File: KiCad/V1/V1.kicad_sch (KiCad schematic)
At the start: 3 parts, among them U1 74LS132

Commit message: kicad scematic
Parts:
- removed R_load: R, symbol Device:R
- added C1, C2, C3, C5, C6, C7, C8: C, symbol Device:C
- added C4: 20p, symbol Device:C
- added L1, L2: L, symbol Device:L
- added R1: R, symbol Device:R
- added R2, R3: 100, symbol Device:R
- added R4, R5: 250, symbol Device:R
- added R6, R7: 0, symbol Device:R
- added R8: NOMCT16031001AT1, NOMC16_VIS, symbol 2024-11-17_18-44-26:NOMCT16031001AT1
- added RV1: R_Potentiometer, symbol Device:R_Potentiometer
- added RV2: 1k, symbol Device:R_Potentiometer
- added U2, U3: OPA2677IDDA, DDA8_3X2P49, symbol 2024-11-17_16-46-04:OPA2677IDDA
- added U4: OPA855QDSGRQ1, WSON8_DSG_TEX, symbol 2024-11-17_18-04-17:OPA855QDSGRQ1
- renumbered R_shutn to R_shutn1
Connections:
- net V_sens: now reaches U1.1
- net V_sens: now also R8.1, U4.6 (OUT)
- net V_ref: now reaches U1.2
- net at U1.3: now also RV2.2
- net -Shunt: now reaches R_shutn1.2
- net -Shunt: now also R8.2
- net Filter/Filter_OUT renamed +Shunt
- net +Shunt: now also L2.2, R8.3
- new net: R2.1, R3.2, U2.2 (INA-)
- new net: C1.1, R1.1
- new net: L1.2, L2.1, R1.2
- new net: R8.13, R8.14, U4.4 (IN+)
- new net: R8.15, R8.16, U4.3 (IN-)
- new net: R6.2, R7.1, U3.4 (VS-)
- new net: R4.1, RV1.1, U2.3 (INA+)
- new net: C4.2, RV1.2, U2.7 (OUTB), U3.2 (INA-)
- new net: R4.2, R5.2, U2.1 (OUTA)
- new net: C4.1, R5.1, U2.6 (INB-)
- new net +5V: C2.2, C3.2, C5.2, C6.2, C7.2, C8.2, R3.1, U2.8 (VS+), U3.7 (OUTB), U4.7 (VS+)
- new net -1V: R6.1
- new net Controll PWM: U3.1 (OUTA)
- new net GND: C1.2, C2.1, C3.1, C5.1, C6.1, C7.1, C8.1, R2.2, R7.2, R8.4, RV2.3, U2.4 (VS-), U2.5 (INB+), U2.EPAD, U3.8 (VS+), U4.5 (VS-), U4.9 (EPAD)
- new net PWM: L1.1
- new net V_Controll: U3.3 (INA+)
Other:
- removed sheet Current Sense
- removed sheet Driver
- removed sheet Filter
- removed sheet PWM Generator
- note added: "Controller"
- note added: "Filter and Sensor"
- note added: "PWM Generator"
- moved on the sheet: R_shutn1, U1A

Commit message: asdaslkwrjhsoid7ty
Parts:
- C1: value C -> 70p; footprint (none) -> Capacitor_SMD:C_0402_1005Metric
- C2, C3, C4, C5, C6, C7, C8: footprint (none) -> Capacitor_SMD:C_0402_1005Metric
- L1, L2: value L -> 1u
- R1: value R -> 200
- R2, R3, R4, R5: footprint (none) -> Resistor_SMD:R_0402_1005Metric
- R6, R7: footprint (none) -> Resistor_SMD:R_0805_2012Metric
- R_shutn1: value R -> 0.1
- U2, U3: footprint DDA8_3X2P49 -> footprints:DDA8_3X2P49
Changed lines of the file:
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@@
 			)
 		)
-		(property "Footprint" ""
+		(property "Footprint" "Resistor_SMD:R_0402_1005Metric"
 			(at 44.45 202.692 90)
 			(effects
@@
 			)
 		)
-		(property "Value" "C"
+		(property "Value" "70p"
 			(at 49.53 78.7399 0)
 			(effects
@@
 			)
 		)
-		(property "Footprint" ""
+		(property "Footprint" "Capacitor_SMD:C_0402_1005Metric"
 			(at 46.6852 81.28 0)
 			(effects
@@
 			)
 		)
-		(property "Footprint" ""
+		(property "Footprint" "Capacitor_SMD:C_0402_1005Metric"
 			(at 129.8448 187.96 0)
 			(effects
@@
 			)
 		)
-		(property "Value" "R"
+		(property "Value" "0.1"
 			(at 71.12 57.15 90)
 			(effects
@@
 			)
 		)
-		(property "Value" "R"
+		(property "Value" "200"
 			(at 48.26 69.8499 0)
 			(effects
@@
 			)
 		)
-		(property "Footprint" ""
+		(property "Footprint" "Capacitor_SMD:C_0402_1005Metric"
 			(at 188.2648 196.85 0)
 			(effects
@@
 			)
 		)
-		(property "Value" "L"
+		(property "Value" "1u"
 			(at 54.61 58.42 90)
 			(effects
@@
 			)
 		)
-		(property "Footprint" ""
+		(property "Footprint" "Resistor_SMD:R_0805_2012Metric"
 			(at 147.32 229.108 90)
 			(effects
@@
 			)
 		)
-		(property "Value" "L"
+		(property "Value" "1u"
 			(at 38.1 58.42 90)
 			(effects
@@
 			)
 		)
-		(property "Footprint" ""
+		(property "Footprint" "Capacitor_SMD:C_0402_1005Metric"
 			(at 179.3748 196.85 0)
 			(effects
@@
 			)
 		)
-		(property "Footprint" ""
+		(property "Footprint" "Capacitor_SMD:C_0402_1005Metric"
 			(at 197.1548 196.85 0)
 			(effects
@@
 			)
 		)
-		(property "Footprint" "DDA8_3X2P49"
+		(property "Footprint" "footprints:DDA8_3X2P49"
 			(at 69.85 201.93 0)
 			(effects
@@
 			)
 		)
-		(property "Footprint" ""
+		(property "Footprint" "Resistor_SMD:R_0402_1005Metric"
 			(at 57.658 212.09 90)
 			(effects
@@
 			)
 		)
-		(property "Footprint" ""
+		(property "Footprint" "Capacitor_SMD:C_0402_1005Metric"
 			(at 120.9548 187.96 0)
 			(effects
@@
 			)
 		)
-		(property "Footprint" ""
+		(property "Footprint" "Resistor_SMD:R_0402_1005Metric"
 			(at 46.482 200.66 90)
 			(effects
@@
 			)
 		)
-		(property "Footprint" ""
+		(property "Footprint" "Resistor_SMD:R_0805_2012Metric"
 			(at 141.478 231.14 90)
 			(effects
@@
 			)
 		)
-		(property "Footprint" ""
+		(property "Footprint" "Capacitor_SMD:C_0402_1005Metric"
 			(at 112.0648 187.96 0)
 			(effects
@@
 			)
 		)
-		(property "Footprint" ""
+		(property "Footprint" "Capacitor_SMD:C_0402_1005Metric"
 			(at 122.2248 207.01 0)
 			(effects
@@
 			)
 		)
-		(property "Footprint" ""
+		(property "Footprint" "Resistor_SMD:R_0402_1005Metric"
 			(at 112.268 199.39 90)
 			(effects
@@
 			)
 		)
-		(property "Footprint" "DDA8_3X2P49"
+		(property "Footprint" "footprints:DDA8_3X2P49"
 			(at 139.7 208.28 0)
 			(effects

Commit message: kicad scematic
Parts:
- removed U1: 74LS132, symbol 74xx:74LS132
- added R9: NOMCT16031001AT1, NOMC16_VIS, symbol 2024-11-17_18-44-26:NOMCT16031001AT1
- added U5: OPA855QDSGRQ1, WSON8_DSG_TEX, symbol 2024-11-17_18-04-17:OPA855QDSGRQ1
- C4: value 20p -> 30p
- R4, R5: value 250 -> 150
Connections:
- net +5V: now also U5.7 (VS+)
- net +Shunt: now also R8.8; no longer R8.3
- net -Shunt: no longer R8.2, R_shutn1.2
- net GND: now also R8.7, R9.7, U5.5 (VS-), U5.9 (EPAD); no longer R8.4
- net PWM: now also RV2.1
- net V_sens: now also R8.2, R9.1; no longer R8.1
- net at RV2.2: now also R9.2, U5.6 (OUT)
- net at R8.10: now also R8.11
- net at R8.12: now also R8.9, U4.4 (IN+)
- net at R8.16, U4.3 (IN-): now also R8.13; no longer R8.15
- net at R8.5: now also R8.6
- new net: R9.10, R9.11
- new net: R9.14, R9.15
- new net: R9.3, R9.4
- new net: R9.5, R9.6
- new net: R8.14, R8.15
- new net: R8.3, R8.4
- new net OUT: R8.1, R_shutn1.2
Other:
- note added: "Short here for 1/1 Gain ->"
- moved on the sheet: C1, L1, L2, R1, R8, RV2, R_shutn1, U4

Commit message: Worked on V1 PCB
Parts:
- removed R3: 100, Resistor_SMD:R_0402_1005Metric, symbol Device:R
- added C10, C15, C17, C18, C19: 1u, Capacitor_SMD:C_0402_1005Metric, symbol Device:C
- added C11: 10u, Capacitor_SMD:C_2220_5750Metric, symbol Device:C
- added C12: 10n, Capacitor_SMD:C_0805_2012Metric, symbol Device:C
- added C13, C14, C16: 10n, Capacitor_SMD:C_0402_1005Metric, symbol Device:C
- added C9: 10u, Capacitor_SMD:C_0603_1608Metric, symbol Device:C
- added D1, D2: D_Schottky, Package_TO_SOT_SMD:SOT-323_SC-70, symbol Device:D_Schottky
- added EN1, VDD10: MountingHole_Pad, TestPoint:TestPoint_THTPad_D2.5mm_Drill1.2mm, symbol Mechanical:MountingHole_Pad
- added GND1, VDD_PWM_BIG1: MountingHole_Pad, MountingHole:MountingHole_2.5mm_Pad_TopBottom, symbol Mechanical:MountingHole_Pad
- added H5, H6, H7, H8: MountingHole_Pad, MountingHole:MountingHole_4.3mm_M4_DIN965_Pad_TopBottom, symbol Mechanical:MountingHole_Pad
- added PWM_IN1, Post_Filter1, Pre_Filter1: Conn_Coaxial, Connector_Coaxial:U.FL_Molex_MCRF_73412-0110_Vertical, symbol Connector:Conn_Coaxial
- added Q1, Q2: Q_NMOS_GSD, MyResistors:EPC8009, symbol Device:Q_NMOS_GSD
- added R10: 150, Resistor_SMD:R_0402_1005Metric, symbol Device:R
- added R12, R14: 47, Resistor_SMD:R_0402_1005Metric, symbol Device:R
- added R15, R16: 0, Capacitor_SMD:C_0805_2012Metric, symbol Device:R
- added RdtH1, RdtL1: 1.8M, Resistor_SMD:R_0402_1005Metric, symbol Device:R
- added U1: LMG1210RVRR, Drivers:IC_LMG1210RVRR, symbol LMG1210RVRR:LMG1210RVRR
- C1: footprint Capacitor_SMD:C_0402_1005Metric -> Resistor_SMD:R_1206_3216Metric
- C2: value C -> 10u
- C3: value C -> 4.7u; footprint Capacitor_SMD:C_0402_1005Metric -> Capacitor_SMD:C_0603_1608Metric
- C4: value 30p -> 27p
- C5, C8: value C -> 10n
- C6: value C -> 10u; footprint Capacitor_SMD:C_0402_1005Metric -> Capacitor_SMD:C_0603_1608Metric
- C7: value C -> 1u
- L1: footprint (none) -> MyFootprints:INductor_744060421
- L2: value 1u -> 1.5u; footprint (none) -> MyFootprints:INductor_744060421
- R1: value 200 -> 47; footprint (none) -> Resistor_SMD:R_0402_1005Metric
- R2: value 100 -> 200; footprint Resistor_SMD:R_0402_1005Metric -> Resistor_SMD:R_1206_3216Metric
- R6, R7: footprint Resistor_SMD:R_0805_2012Metric -> Capacitor_SMD:C_0805_2012Metric
- R8, R9: value NOMCT16031001AT1 -> TOMCT16031002ZT1; footprint NOMC16_VIS -> MyFootprints:TOMCT16031002ZT1
- RV1: value R_Potentiometer -> 200; footprint (none) -> MyFootprints:POT_ 3214W-1-201E
- RV2: value 1k -> 200; footprint (none) -> MyFootprints:POT_ 3214W-1-201E
- R_shutn1: footprint (none) -> Resistor_SMD:R_2512_6332Metric
- U4, U5: value OPA855QDSGRQ1 -> OPA859QDSGRQ1; footprint WSON8_DSG_TEX -> MyFootprints:OPA859QDSGRQ1
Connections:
- net OUT is gone; now on net -Shunt: R8.1, R_shutn1.2
- net +5V: now also C10.2, C16.2, C9.2; no longer C2.2, C3.2, C5.2, U2.8 (VS+), U3.7 (OUTB)
- net -Shunt: now also C13.2
- net GND: now also C3.2, R2.1, R8.5, R9.5, U3.EPAD, C10.1, C11.2, C12.2, C16.1, C17.2, C18.1, C19.1, C9.1, GND1.1, H5.1, H6.1, H7.1, H8.1, PWM_IN1.2 (Ext), Post_Filter1.2 (Ext), Pre_Filter1.2 (Ext), Q2.2 (S), RdtH1.1, RdtL1.1, U1.20 (VSS), U1.20_1 (VSS), U1.20_2 (VSS), U1.3 (VSS), U1.7 (VSS); no longer C1.2, C3.1, R2.2, R8.7, R9.7, U3.8 (VS+)
- net V_ref: now also R9.8
- net V_sens: now also R8.4; no longer R8.2
- net VPWN_Gen/2: now reaches U2.2 (INA-)
- net VPWN_Gen/2: no longer R2.1
- net at C1.1: now also L1.2, L2.1; no longer R1.1
- net at R9.10: now also R9.9; no longer R9.11
- net at R9.12: now also R9.11
- net at R9.13: now also R9.14
- net at R9.15: now also R9.16; no longer R9.14
- net at R9.4: now also RV2.1, U5.6 (OUT); no longer R9.3
- net at R9.6: now also R9.7, U5.4 (IN+); no longer R9.5
- net at R8.10: now also R8.9; no longer R8.11
- net at R8.14: now also R8.13; no longer R8.15
- net at R8.3: now also R8.2, U4.3 (IN-); no longer R8.4
- net at R8.6: now also R8.7, U4.4 (IN+); no longer R8.5
- net at C4.2, U2.7 (OUTB), U3.2 (INA-): now also R10.2; no longer RV1.2
- net at U5.3 (IN-): now also R9.2, R9.3
- net Controll PWM renamed PWM_Small
- net PWM_Small: now also R15.2
- net PWM renamed HS1
- net HS1: now also C14.2, C15.2, Q1.2 (S), Q2.3 (D), U1.13 (HS), U1.14 (NC1), U1.16 (HS), U1.21 (HS), U1.21_1 (HS), U1.21_2 (HS), U1.9 (HS); no longer RV2.1
- net V_Controll renamed V_Error
- net V_Error: now also RV2.2
- new net: R10.1, RV1.2
- new net: RdtH1.2, U1.6 (DLH)
- new net: R8.11, R8.12
- new net: R8.15, R8.16
- new net: C13.1, R12.2
- new net: C14.1, R14.2
- new net: R1.1, R15.1, U1.19 (PWM/LI)
- new net: C1.2, R2.2
- new net: RdtL1.2, U1.5 (DHL)
- new net -VPWM_comp: U3.8 (VS+)
- new net BST1: D1.1 (A), D2.1 (A), U1.17 (BST)
- new net EN1: EN1.1, R16.1, U1.18 (EN/HI)
- new net HB1: C15.1, D1.3 (K), D2.3 (K), U1.12 (HB)
- new net HO1: Q1.1 (G), U1.10 (HO)
- new net LO1: Q2.1 (G), U1.8 (LO)
- new net PWM_External: PWM_IN1.1 (In), R1.2
- new net Post_Filter: Post_Filter1.1 (In), R12.1
- new net Pre_Filter1: Pre_Filter1.1 (In), R14.1
- new net VCC1: C3.1, R16.2, U1.4 (VDD)
- new net VDD10: C19.2, U1.2 (VIN), VDD10.1
- new net VDD_PWM_Big: C11.1, C12.1, C17.1, Q1.3 (D), VDD_PWM_BIG1.1
- new net VPWN_Gen: C18.2, C2.2, C5.2, U2.8 (VS+), U3.7 (OUTB)
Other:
- note added: "PWM Amplifier"
- note added: "TODO * Check LMG1210 Rise time ressistors * POwer supply (5V 4V 2V 1V 10V)"
- note removed: "Short here for 1/1 Gain ->"
- moved on the sheet: C2, C4, C5, L1, L2, R4, R5, R7, RV2, U2, U3, U5

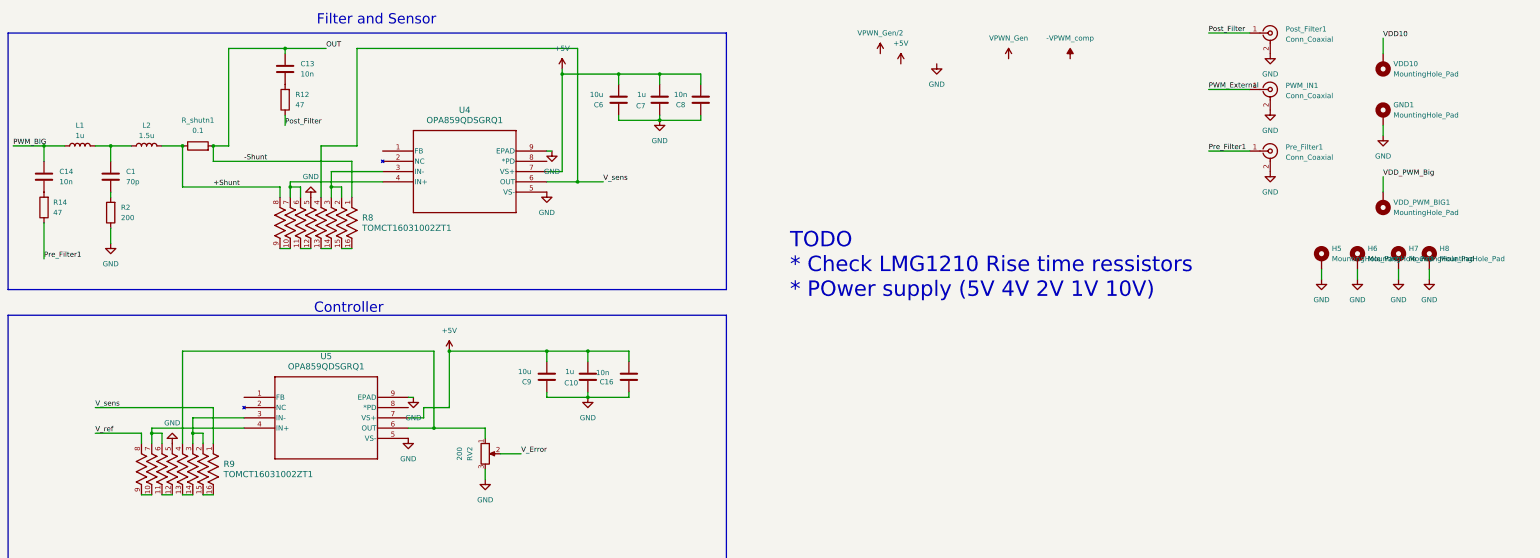
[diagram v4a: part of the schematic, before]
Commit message: added integrator
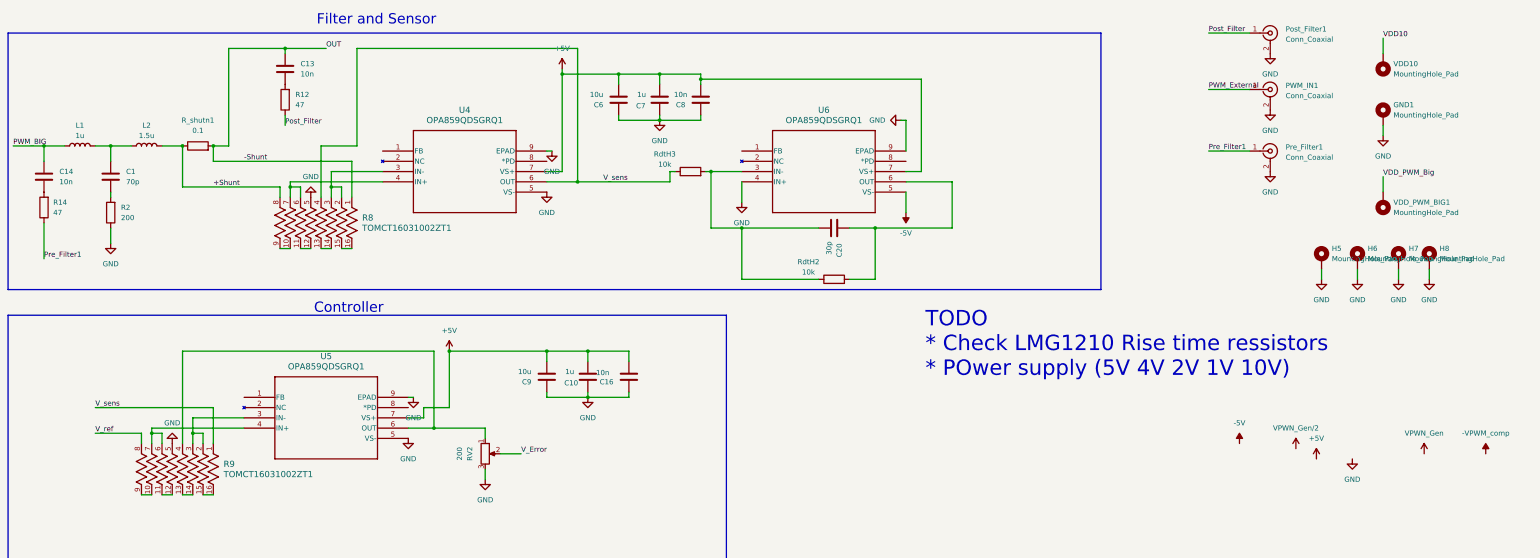
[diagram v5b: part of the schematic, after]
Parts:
- added C20: 30p, Capacitor_SMD:C_0402_1005Metric, symbol Device:C
- added RdtH2, RdtH3: 10k, Resistor_SMD:R_0402_1005Metric, symbol Device:R
- added U6: OPA859QDSGRQ1, MyFootprints:OPA859QDSGRQ1, symbol 2024-11-17_18-04-17:OPA855QDSGRQ1
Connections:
- net +5V: now also U6.7 (VS+)
- net GND: now also U6.4 (IN+), U6.9 (EPAD)
- net V_sens: now also RdtH3.1
- new net: C20.1, RdtH2.2, U6.6 (OUT)
- new net: C20.2, RdtH2.1, RdtH3.2, U6.3 (IN-)
- new net -5V: U6.5 (VS-)

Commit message: eddit
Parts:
- removed R10: 150, Resistor_SMD:R_0402_1005Metric, symbol Device:R
- removed R7: 0, Capacitor_SMD:C_0805_2012Metric, symbol Device:R
- added C21: 10u, Capacitor_SMD:C_0402_1005Metric, symbol Device:C
- added C22: 1u, Capacitor_SMD:C_0402_1005Metric, symbol Device:C
- added C23: 10n, Capacitor_SMD:C_0402_1005Metric, symbol Device:C
- added R3: 0, Capacitor_SMD:C_0805_2012Metric, symbol Device:R
- C20: now not fitted
- R1, R12, R14: value 47 -> 49.9
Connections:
- net VPWN_Gen/2 is gone; now on net GND: U2.2 (INA-)
- net +5V: now also U3.7 (OUTB), C21.2, C22.2, C23.2; no longer C10.2, C16.2, C9.2, U5.7 (VS+)
- net -1V: now also R3.1; no longer R6.1
- net GND: now also R6.2, C21.1, C22.1, C23.1; no longer U2.4 (VS-), U5.5 (VS-)
- net VPWN_Gen: no longer C18.2, C2.2, C5.2, U2.8 (VS+), U3.7 (OUTB)
- net V_sens: now also C20.1, RdtH2.2, U6.6 (OUT); no longer R8.4, RdtH3.1, U4.6 (OUT)
- net at RV1.2: now also C4.2, U2.7 (OUTB), U3.2 (INA-)
- net at U3.4 (VS-): now also R6.1, R3.2; no longer R6.2
- net +Shunt: no longer names the net of L2.2, R_shutn1.1
- net +Shunt: now also R8.1; no longer R8.8
- net -Shunt renamed OUT
- net OUT: now also R8.8; no longer R8.1
- new net: R8.4, RdtH3.1, U4.6 (OUT)
- new net +2V: C10.2, C16.2, C9.2, U5.7 (VS+)
- new net -2V: U2.4 (VS-), U5.5 (VS-)
- new net 2V: C18.2, C2.2, C5.2, U2.8 (VS+)
